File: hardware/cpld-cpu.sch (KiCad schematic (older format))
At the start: 386 parts, among them J1 Acc, J10 Page, J11 PC_H, J12 Conn_02x16_Odd_Even, J13 Page, J14 Conn_02x16_Odd_Even, J2 X, J3 IR, J4 AXM, J5 Dec, J6 AR, J7 ALU, J8 Index, J9 PC_L, SW1 BTN0, SW2 BTN0, SW3 BTN0, U1 Acc, U10 RAM_Page, U11 PC_H, U12 CY62138FV30LL, U13 GPIO_RNG, U2 X, U3 IR, U4 Multiplexer, U5 Decoder, U6 AR, U7 ALU, U8 RAM_Index, U9 PC_L

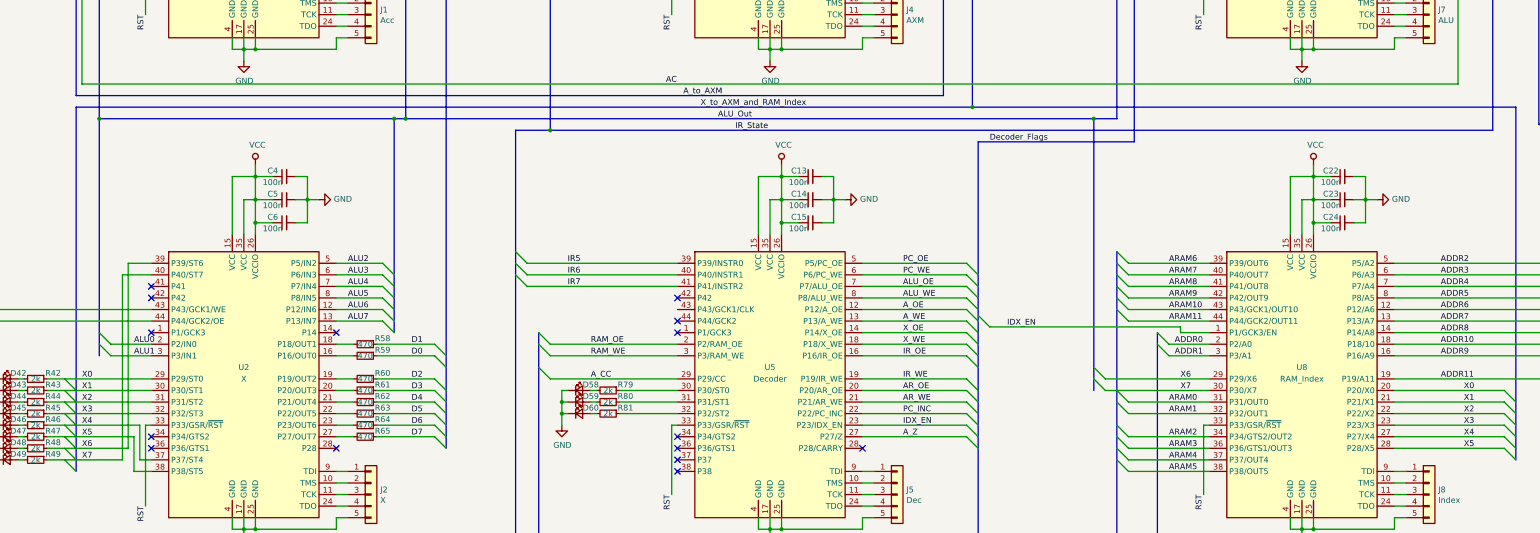
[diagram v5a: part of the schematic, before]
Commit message: VHDL for ioregister and program_counter.
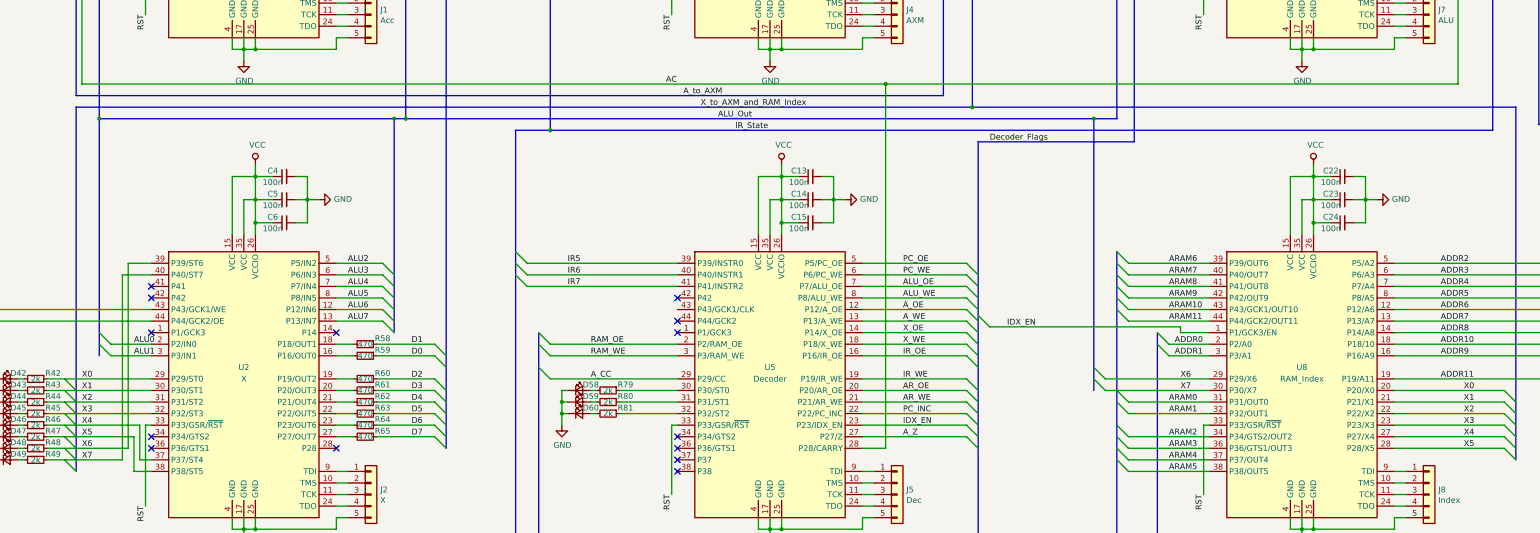
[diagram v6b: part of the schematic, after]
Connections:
- net AC: now also U5.28 (P28/CARRY)
- no-connect marks 67 -> 66
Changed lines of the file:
@@
 	1    0    0    -1
 $EndComp
-NoConn ~ 9100 7700
 NoConn ~ 7500 6400
 NoConn ~ 7500 6600
@@
 	2350 3750 2350 4550
 Wire Wire Line
-	2350 4550 14250 4550
+	2350 4550 9300 4550
 Wire Wire Line
 	14250 4550 14250 2550
@@
 Wire Bus Line
 	2300 4750 2300 7900
+Wire Wire Line
+	9300 4550 9300 7700
+Wire Wire Line
+	9300 7700 9100 7700
+Wire Wire Line
+	2050 7700 2750 7700
+Wire Wire Line
+	2050 7400 2950 7400
+Wire Wire Line
+	2050 7800 2700 7800
+Wire Wire Line
+	2050 7600 2800 7600
+Wire Wire Line
+	2050 7500 2850 7500
+Wire Wire Line
+	2050 7300 2950 7300
+Wire Wire Line
+	2050 7200 2950 7200
+Wire Wire Line
+	2050 3550 2750 3550
+Wire Wire Line
+	2050 3250 2950 3250
+Wire Wire Line
+	2050 3650 2700 3650
+Wire Wire Line
+	2050 3450 2800 3450
+Wire Wire Line
+	2050 3350 2850 3350
+Wire Wire Line
+	2050 3150 2950 3150
+Wire Wire Line
+	2050 3050 2950 3050
+Wire Wire Line
+	11200 7200 12100 7200
+Wire Wire Line
+	1050 2550 2950 2550
 Wire Bus Line
-	18800 6500 18800 9150
-Wire Bus Line
-	11300 1850 11300 4850
+	2500 2550 2500 4850
+Wire Wire Line
+	2050 2950 2950 2950
+Wire Wire Line
+	2050 7100 2950 7100
 Wire Bus Line
-	19100 10200 19100 14550
+	7100 12150 7100 14750
 Wire Bus Line
-	10100 5050 10100 9900
+	3000 12150 3000 14750
 Wire Bus Line
-	5500 650  5500 7700
+	11450 2250 11450 5050
 Wire Bus Line
-	16000 1700 16000 4250
+	11650 6700 11650 8900
 Wire Bus Line
-	26600 7950 26600 9700
+	15650 6400 15650 8550
 Wire Bus Line
-	600  650  600  14750
+	10550 12050 10550 14350
 Wire Bus Line
-	2900 8500 2900 9900
+	15150 9900 15150 12050
 Wire Bus Line
-	15450 6100 15450 8900
+	7000 9900 7000 12050
 Wire Bus Line
-	6750 850  6750 3750
+	6300 6700 6300 9900
 Wire Bus Line
-	2900 9900 2900 12050
+	11600 850  11600 2750
 Wire Bus Line
-	2350 11250 2350 14350
+	2500 4850 2500 6900
 Wire Bus Line
-	6450 10250 6450 14350
+	11100 4850 11100 7200
 Wire Bus Line
-	11300 6000 11300 9150
+	15800 4900 15800 6900
 Wire Bus Line
-	14700 650  14700 3550
+	22000 4900 22000 6900
 Wire Bus Line
-	10050 12150 10050 14550
+	15550 2900 15550 4900
 Wire Bus Line
-	14850 11550 14850 14350
+	18950 11550 18950 14350
 Wire Bus Line
-	14650 12150 14650 14550
+	11200 9900 11200 12150
 Wire Bus Line
-	9800 1950 9800 4650
+	6100 4950 6100 9500
 Wire Bus Line
-	10050 2750 10050 4750
+	18950 4900 18950 6500
 Wire Bus Line
-	5150 1950 5150 4850
+	25000 9150 25000 9500
 Wire Bus Line
-	24750 6700 24750 7950
+	5950 12350 5950 14550
 Wire Bus Line
-	25050 6850 25050 9000
+	6200 11550 6200 14750
 Wire Bus Line
-	19100 1800 19100 4250
+	10300 11550 10300 14750
 Wire Bus Line
-	18650 2800 18650 4900
+	950  2150 950  8500
 Wire Bus Line
-	25150 4900 25150 6850
+	14400 850  14400 2550
 Wire Bus Line
-	16000 4250 16000 7800
+	5050 4850 5050 6700
 Wire Bus Line
 	14750 4750 14750 7800
 Wire Bus Line
-	5050 4850 5050 6700
+	16000 4250 16000 7800
 Wire Bus Line
-	14400 850  14400 2550
+	25150 4900 25150 6850
 Wire Bus Line
-	950  2150 950  8500
+	18650 2800 18650 4900
 Wire Bus Line
-	10300 11550 10300 14750
+	19100 1800 19100 4250
 Wire Bus Line
-	6200 11550 6200 14750
+	11300 6000 11300 9150
 Wire Bus Line
-	5950 12350 5950 14550
+	14700 650  14700 3550
 Wire Bus Line
-	18950 11550 18950 14350
+	10050 12150 10050 14550
 Wire Bus Line
-	11200 9900 11200 12150
+	14850 11550 14850 14350
 Wire Bus Line
-	6100 4950 6100 9500
+	14650 12150 14650 14550
 Wire Bus Line
-	18950 4900 18950 6500
+	9800 1950 9800 4650
 Wire Bus Line
-	25000 9150 25000 9500
-Wire Wire Line
-	2050 7700 2750 7700
-Wire Wire Line
-	2050 7400 2950 7400
-Wire Wire Line
-	2050 7800 2700 7800
-Wire Wire Line
-	2050 7600 2800 7600
-Wire Wire Line
-	2050 7500 2850 7500
-Wire Wire Line
-	2050 7300 2950 7300
-Wire Wire Line
-	2050 7200 2950 7200
-Wire Wire Line
-	2050 3550 2750 3550
-Wire Wire Line
-	2050 3250 2950 3250
-Wire Wire Line
-	2050 3650 2700 3650
-Wire Wire Line
-	2050 3450 2800 3450
-Wire Wire Line
-	2050 3350 2850 3350
-Wire Wire Line
-	2050 3150 2950 3150
-Wire Wire Line
-	2050 3050 2950 3050
+	10050 2750 10050 4750
 Wire Bus Line
-	15550 2900 15550 4900
+	5150 1950 5150 4850
 Wire Bus Line
-	22000 4900 22000 6900
+	24750 6700 24750 7950
 Wire Bus Line
-	15800 4900 15800 6900
+	25050 6850 25050 9000
 Wire Bus Line
-	11100 4850 11100 7200
+	6450 10250 6450 14350
 Wire Bus Line
-	2500 4850 2500 6900
+	2350 11250 2350 14350
 Wire Bus Line
-	11600 850  11600 2750
+	2900 9900 2900 12050
 Wire Bus Line
-	6300 6700 6300 9900
+	6750 850  6750 3750
 Wire Bus Line
-	7000 9900 7000 12050
+	15450 6100 15450 8900
 Wire Bus Line
-	15150 9900 15150 12050
+	2900 8500 2900 9900
 Wire Bus Line
-	10550 12050 10550 14350
-Wire Wire Line
-	11200 7200 12100 7200
-Wire Wire Line
-	1050 2550 2950 2550
+	600  650  600  14750
 Wire Bus Line
-	2500 2550 2500 4850
-Wire Wire Line
-	2050 2950 2950 2950
-Wire Wire Line
-	2050 7100 2950 7100
+	26600 7950 26600 9700
 Wire Bus Line
-	7100 12150 7100 14750
+	16000 1700 16000 4250
 Wire Bus Line
-	3000 12150 3000 14750
+	10100 5050 10100 9900
 Wire Bus Line
-	11450 2250 11450 5050
+	5500 650  5500 7700
 Wire Bus Line
-	11650 6700 11650 8900
+	19100 10200 19100 14550
 Wire Bus Line
-	15650 6400 15650 8550
+	11300 1850 11300 4850
+Wire Bus Line
+	18800 6500 18800 9150
+Connection ~ 9300 4550
+Wire Wire Line
+	9300 4550 14250 4550
 $EndSCHEMATC

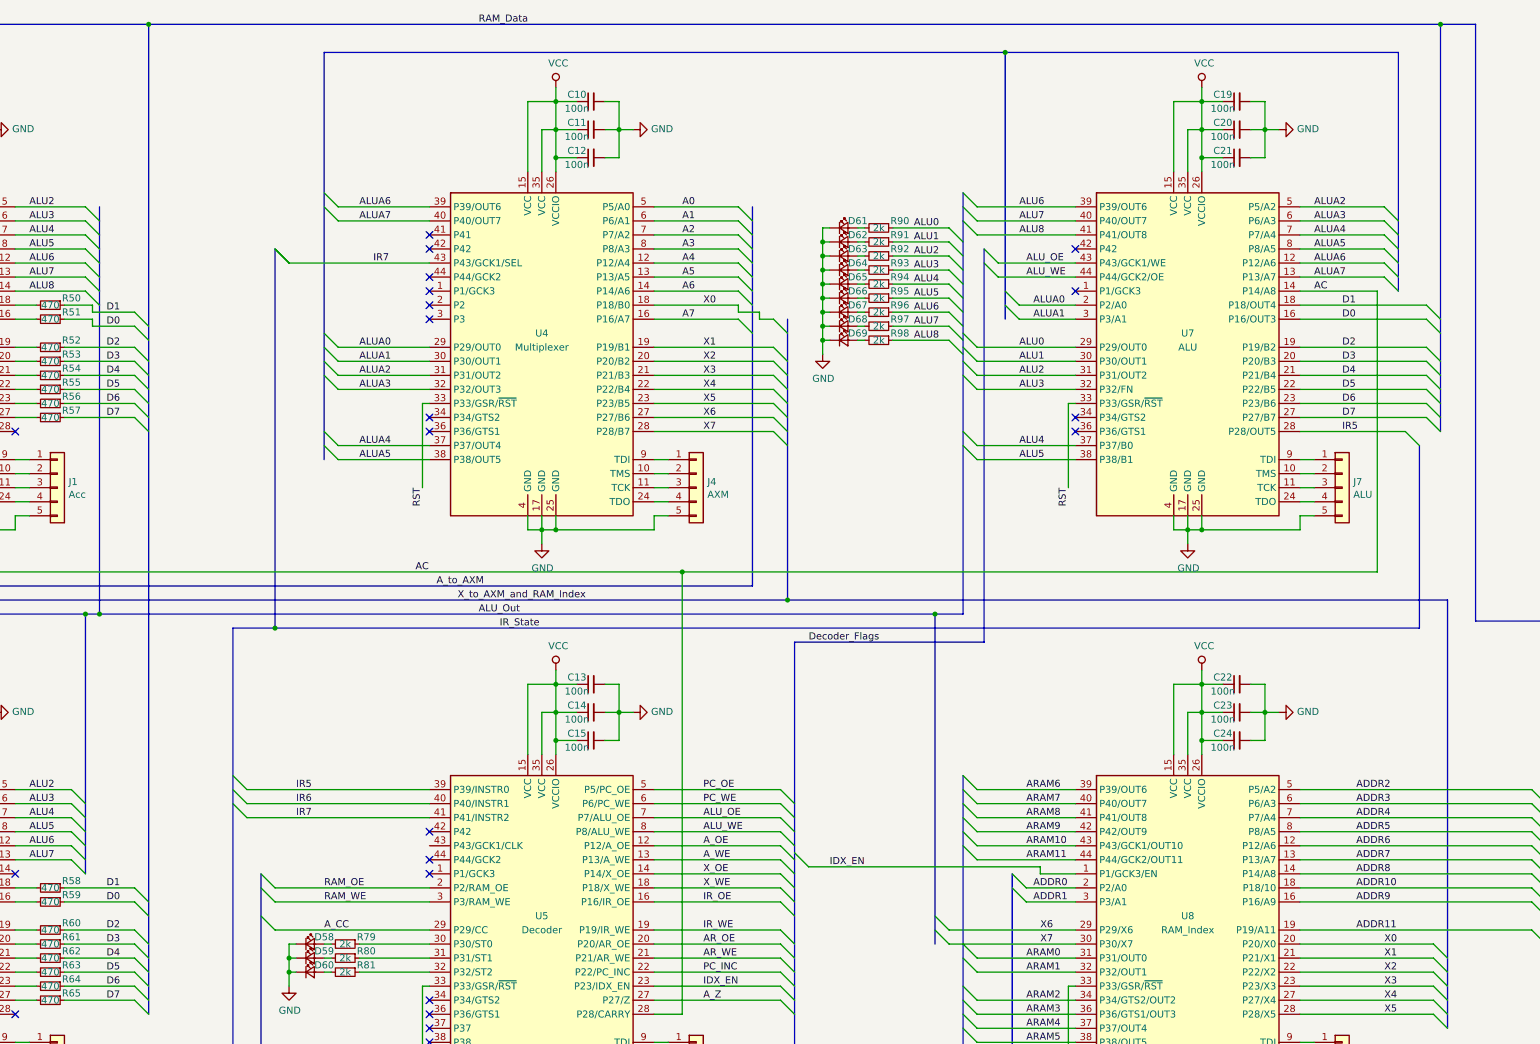
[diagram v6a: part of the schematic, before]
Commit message: VHDL for alu/decoder/multiplexer
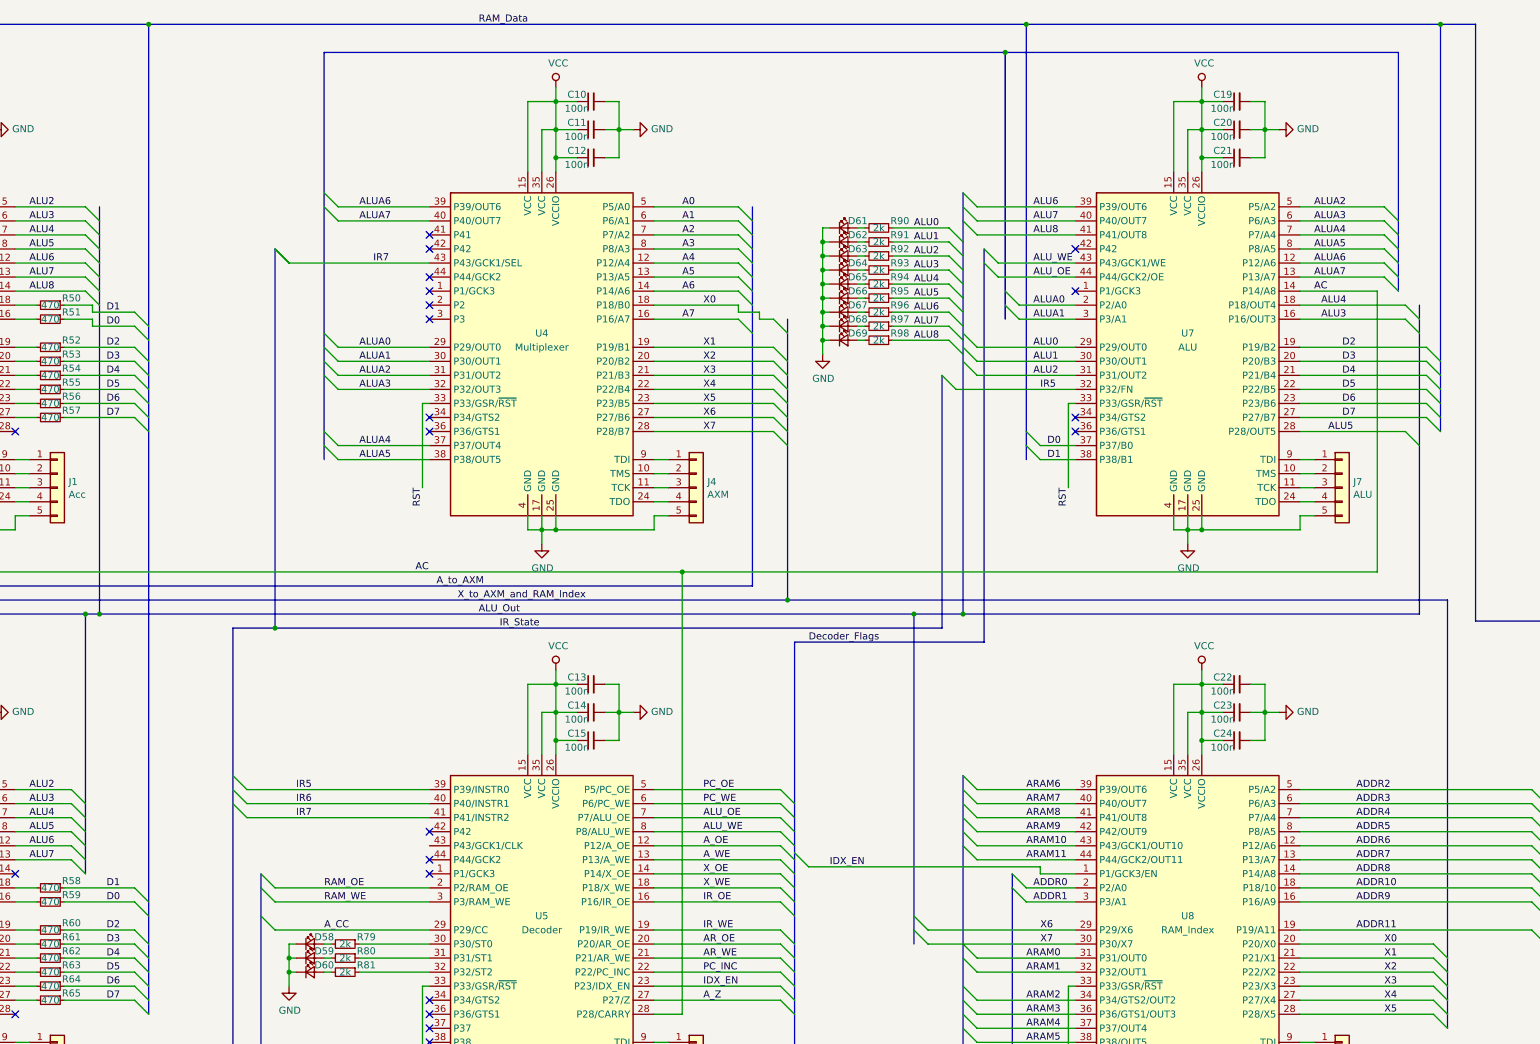
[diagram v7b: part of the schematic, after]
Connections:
- net ALU3: now also U7.16 (P16/OUT3); no longer U7.32 (P32/FN)
- net ALU4: now also U7.18 (P18/OUT4); no longer U7.37 (P37/B0)
- net ALU5: now also U7.28 (P28/OUT5); no longer U7.38 (P38/B1)
- net ALU_OE: now also U7.44 (P44/GCK2/OE); no longer U7.43 (P43/GCK1/WE)
- net ALU_WE: now also U7.43 (P43/GCK1/WE); no longer U7.44 (P44/GCK2/OE)
- net D0: now also U7.37 (P37/B0); no longer U7.16 (P16/OUT3)
- net D1: now also U7.38 (P38/B1); no longer U7.18 (P18/OUT4)
- net IR5: now also U7.32 (P32/FN); no longer U7.28 (P28/OUT5)
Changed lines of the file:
@@
 AC
 Wire Bus Line
-	5500 650  14700 650
-Wire Wire Line
-	13700 2650 14600 2650
-Entry Wire Line
-	14600 2650 14700 2750
-Text Label 14000 2750 0    50   ~ 0
+	5500 650  11750 650
+Text Label 11900 3650 0    50   ~ 0
 D0
-Wire Wire Line
-	13700 2750 14600 2750
-Entry Wire Line
-	14600 2750 14700 2850
-Text Label 14000 2650 0    50   ~ 0
+Text Label 11900 3750 0    50   ~ 0
 D1
 Wire Wire Line
@@
 D7
 Wire Bus Line
-	11100 4850 5150 4850
+	10950 4850 5150 4850
 Entry Wire Line
 	2500 2550 2600 2650
@@
 Wire Wire Line
 	11400 2150 12100 2150
-Text Label 11700 1950 0    50   ~ 0
+Text Label 11800 1950 0    50   ~ 0
 ALU6
-Text Label 11700 2050 0    50   ~ 0
+Text Label 11800 2050 0    50   ~ 0
 ALU7
-Text Label 11700 2150 0    50   ~ 0
+Text Label 11800 2150 0    50   ~ 0
 ALU8
 Entry Wire Line
@@
 Entry Wire Line
 	11300 3050 11400 3150
-Entry Wire Line
-	11300 3150 11400 3250
-Text Label 11700 2950 0    50   ~ 0
+Text Label 11800 2950 0    50   ~ 0
 ALU0
-Text Label 11700 3050 0    50   ~ 0
+Text Label 11800 3050 0    50   ~ 0
 ALU1
-Text Label 11700 3150 0    50   ~ 0
+Text Label 11800 3150 0    50   ~ 0
 ALU2
-Text Label 11700 3250 0    50   ~ 0
+Text Label 13850 2750 0    50   ~ 0
 ALU3
 NoConn ~ 12100 3450
 NoConn ~ 12100 3550
-Entry Wire Line
-	11300 3650 11400 3750
-Entry Wire Line
-	11300 3550 11400 3650
-Text Label 11700 3650 0    50   ~ 0
+Text Label 13850 2650 0    50   ~ 0
 ALU4
-Text Label 11700 3750 0    50   ~ 0
+Text Label 13900 3550 0    50   ~ 0
 ALU5
 NoConn ~ 12100 2550
 NoConn ~ 12100 2250
 Wire Bus Line
-	14550 4950 14550 3650
-Wire Bus Line
 	6100 4950 6400 4950
 Entry Wire Line
-	14450 3550 14550 3650
-Wire Wire Line
-	13700 3550 14450 3550
-Text Label 14000 3550 0    50   ~ 0
+	11150 3150 11250 3250
+Text Label 11850 3250 0    50   ~ 0
 IR5
 Wire Bus Line
@@
 Connection ~ 6400 4950
 Wire Bus Line
-	6400 4950 14550 4950
+	6400 4950 11150 4950
 Entry Wire Line
 	6400 2250 6500 2350
@@
 Wire Wire Line
 	12100 2450 11550 2450
-Text Label 11750 2350 0    50   ~ 0
-ALU_OE
-Text Label 11750 2450 0    50   ~ 0
+Text Label 11800 2350 0    50   ~ 0
 ALU_WE
+Text Label 11800 2450 0    50   ~ 0
+ALU_OE
 NoConn ~ 7500 6700
 Wire Wire Line
@@
 Connection ~ 10050 4750
 Entry Wire Line
-	11100 7000 11200 7100
+	10950 7000 11050 7100
 Entry Wire Line
-	11100 7100 11200 7200
+	10950 7100 11050 7200
 Wire Wire Line
-	11200 7100 12100 7100
+	11050 7100 12100 7100
 Entry Wire Line
 	14650 7200 14750 7300
@@
 	10050 4750 14750 4750
 Wire Bus Line
-	11100 4850 11300 4850
-Connection ~ 11100 4850
+	10950 4850 11300 4850
+Connection ~ 10950 4850
 Wire Bus Line
 	6750 850  11600 850
@@
 	11600 850  14400 850
 Wire Wire Line
-	11400 3650 12100 3650
-Wire Wire Line
 	11400 2950 12100 2950
 Wire Wire Line
@@
 Wire Wire Line
 	11400 3150 12100 3150
-Wire Wire Line
-	11400 3250 12100 3250
-Wire Wire Line
-	11400 3750 12100 3750
 $Comp
 L Device:LED_Small D104
@@
 Wire Wire Line
 	9300 7700 9100 7700
+Connection ~ 9300 4550
+Wire Wire Line
+	9300 4550 14250 4550
+Wire Bus Line
+	11150 3150 11150 4950
+Wire Wire Line
+	11250 3250 12100 3250
+Connection ~ 11750 650
+Wire Bus Line
+	11750 650  14700 650
+Entry Wire Line
+	11750 3550 11850 3650
+Entry Wire Line
+	11750 3650 11850 3750
+Wire Wire Line
+	11850 3650 12100 3650
+Wire Wire Line
+	11850 3750 12100 3750
+Wire Bus Line
+	11300 4850 14550 4850
+Connection ~ 11300 4850
+Wire Wire Line
+	13700 3550 14450 3550
+Entry Wire Line
+	14450 3550 14550 3650
+Entry Wire Line
+	14450 2650 14550 2750
+Entry Wire Line
+	14450 2750 14550 2850
+Wire Wire Line
+	13700 2650 14450 2650
+Wire Wire Line
+	14450 2750 13700 2750
 Wire Wire Line
 	2050 7700 2750 7700
@@
 	2050 3050 2950 3050
 Wire Wire Line
-	11200 7200 12100 7200
+	11050 7200 12100 7200
 Wire Wire Line
 	1050 2550 2950 2550
@@
 	2500 4850 2500 6900
 Wire Bus Line
-	11100 4850 11100 7200
+	10950 4850 10950 7200
 Wire Bus Line
 	15800 4900 15800 6900
@@
 	15550 2900 15550 4900
 Wire Bus Line
+	11750 650  11750 3750
+Wire Bus Line
+	14550 2650 14550 4850
+Wire Bus Line
 	18950 11550 18950 14350
 Wire Bus Line
@@
 	14400 850  14400 2550
 Wire Bus Line
+	14700 650  14700 3550
+Wire Bus Line
 	5050 4850 5050 6700
 Wire Bus Line
@@
 	11300 6000 11300 9150
 Wire Bus Line
-	14700 650  14700 3550
-Wire Bus Line
 	10050 12150 10050 14550
 Wire Bus Line
@@
 	600  650  600  14750
 Wire Bus Line
+	11300 1850 11300 4850
+Wire Bus Line
 	26600 7950 26600 9700
 Wire Bus Line
@@
 	19100 10200 19100 14550
 Wire Bus Line
-	11300 1850 11300 4850
-Wire Bus Line
 	18800 6500 18800 9150
-Connection ~ 9300 4550
-Wire Wire Line
-	9300 4550 14250 4550
 $EndSCHEMATC
